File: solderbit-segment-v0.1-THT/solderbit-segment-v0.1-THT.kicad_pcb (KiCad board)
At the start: 2 copper layers, 25 x 50 mm, 15 parts, among them J1 Conn_01x05_Pin, U1 PCF8574AT, U2 PCF8574N

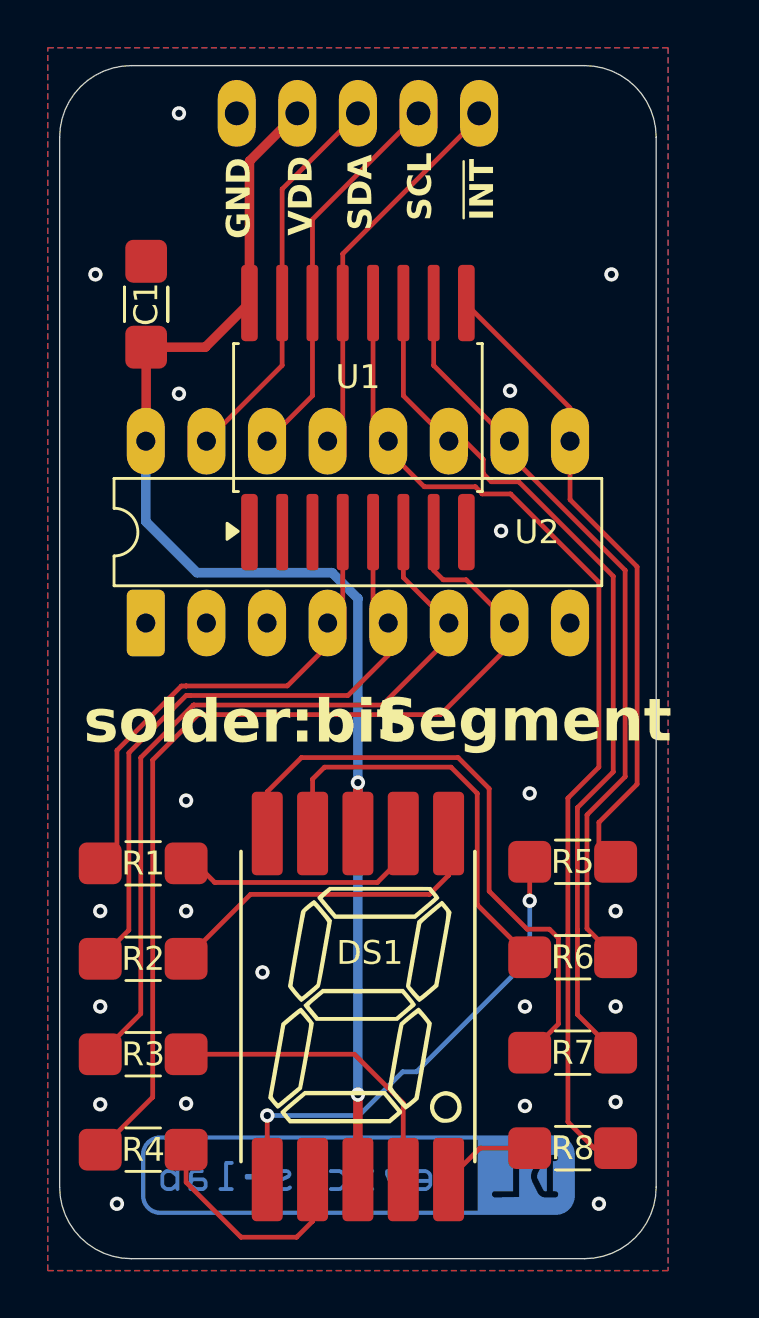
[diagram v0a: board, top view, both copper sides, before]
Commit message: PCB with dual footprints
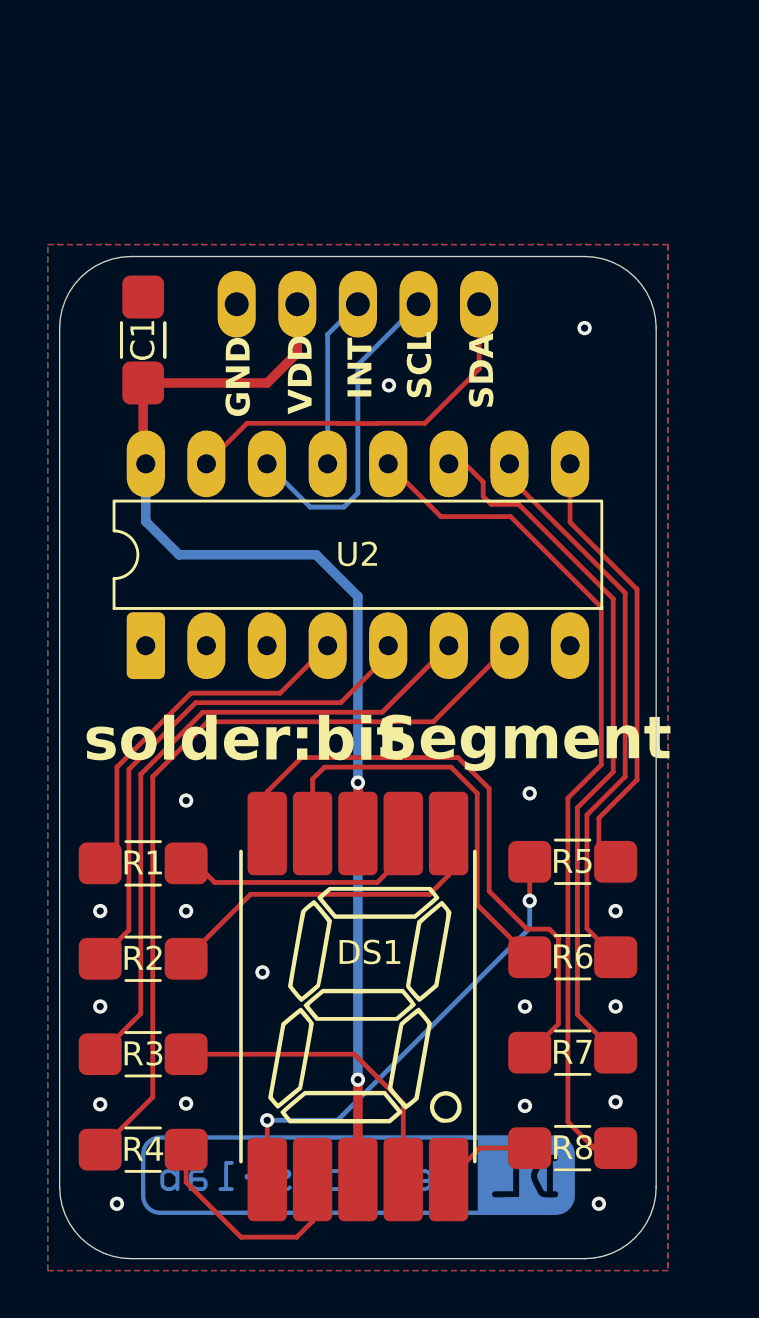
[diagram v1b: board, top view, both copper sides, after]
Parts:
- removed U1: PCF8574AT, SolderbitSegment:SO-16
- moved J1 8.00 mm to (145.1, 67.0)
- moved C1 1.51 mm to (131.0, 68.5)
- moved U2 0.95 mm to (131.1, 81.3)
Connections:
- J1 pad 1: /~{INT} -> /SDA
- J1 pad 3: /SDA -> /~{INT}
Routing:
- net /~{INT}: track 16.4 -> 7.22 mm
- net /P4: track 27.4 -> 18.8 mm
- net /P5: track 31.9 -> 23.8 mm
- net /P6: track 37.4 -> 29.9 mm
- net /P7: track 43.2 -> 36.0 mm
- net /P3: track 40.8 -> 33.8 mm
- net /P2: track 33.3 -> 27.6 mm
- net /P1: track 27.1 -> 21.7 mm
- net /P0: track 20.7 -> 15.3 mm
- net VDD: track 57.0 -> 51.6 mm
- net /SCL: track 16.4 -> 13.8 mm
- net Net-(DS1-E): track 20.5 -> 19.6 mm
- net /SDA: track 16.4 -> 15.8 mm
- net GND: vias 21 -> 17
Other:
- board size 25 x 50 mm -> 25 x 42 mm
- board text added: "INT"
- board text removed: "~{INT}"
